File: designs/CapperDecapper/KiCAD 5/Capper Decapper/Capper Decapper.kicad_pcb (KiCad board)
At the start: 4 copper layers, 77.5 x 42.5 mm, 86 parts, among them J1 Pi Control Signals, J2 Motor_Power, J3 Screw_Term, Q1 Q_NMOS_GSD, U1 INA214, U10 74AHC08, U11 DRV8833RTY, U12 INA214, U13 INA214, U14 V7805-1500R, U15 74AHC08, U16 DRV8833RTY, U17 MAX6018BEUR16, U18 INA214, U19 AP1501A, U2 74AHC08, U3 DRV8833RTY, U4 INA214, U5 INA214, U6 74AHC08, U7 DRV8833RTY, U8 INA214, U9 INA214

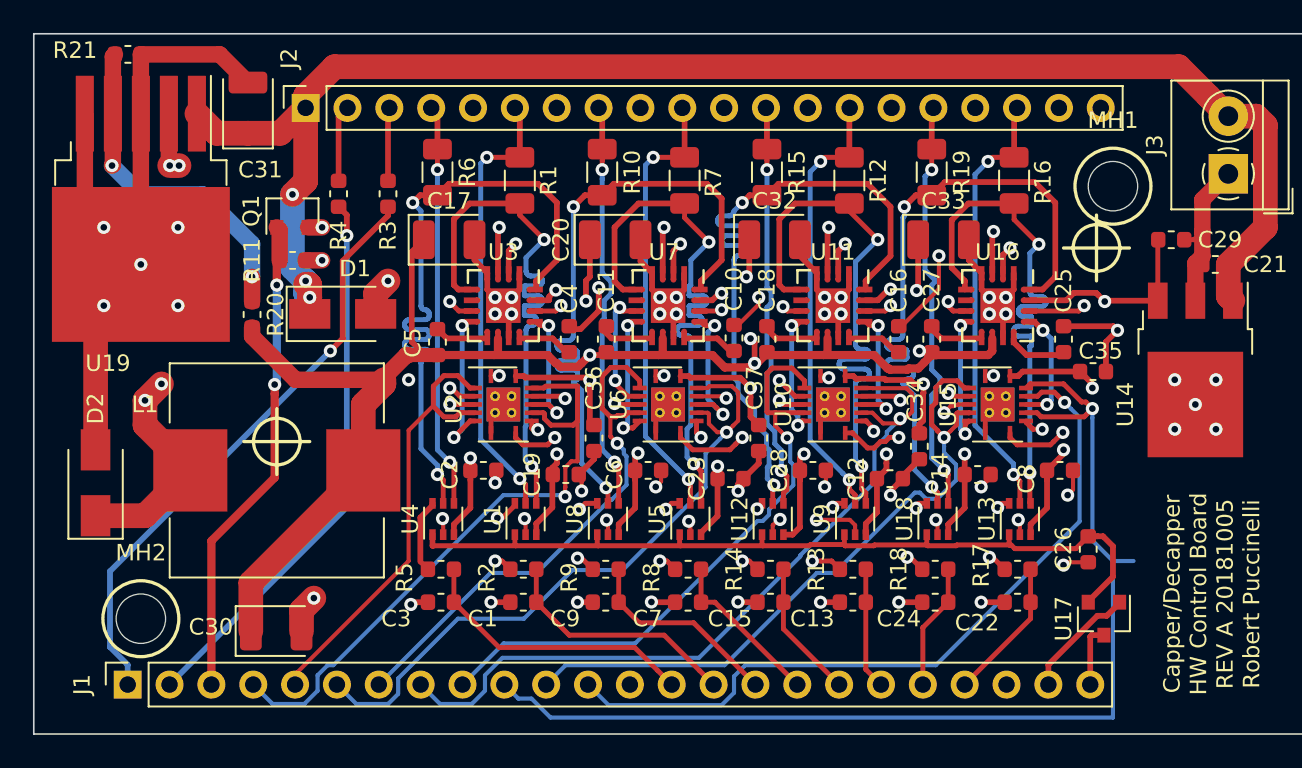
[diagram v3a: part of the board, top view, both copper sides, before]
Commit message: AND gate updated, ordered
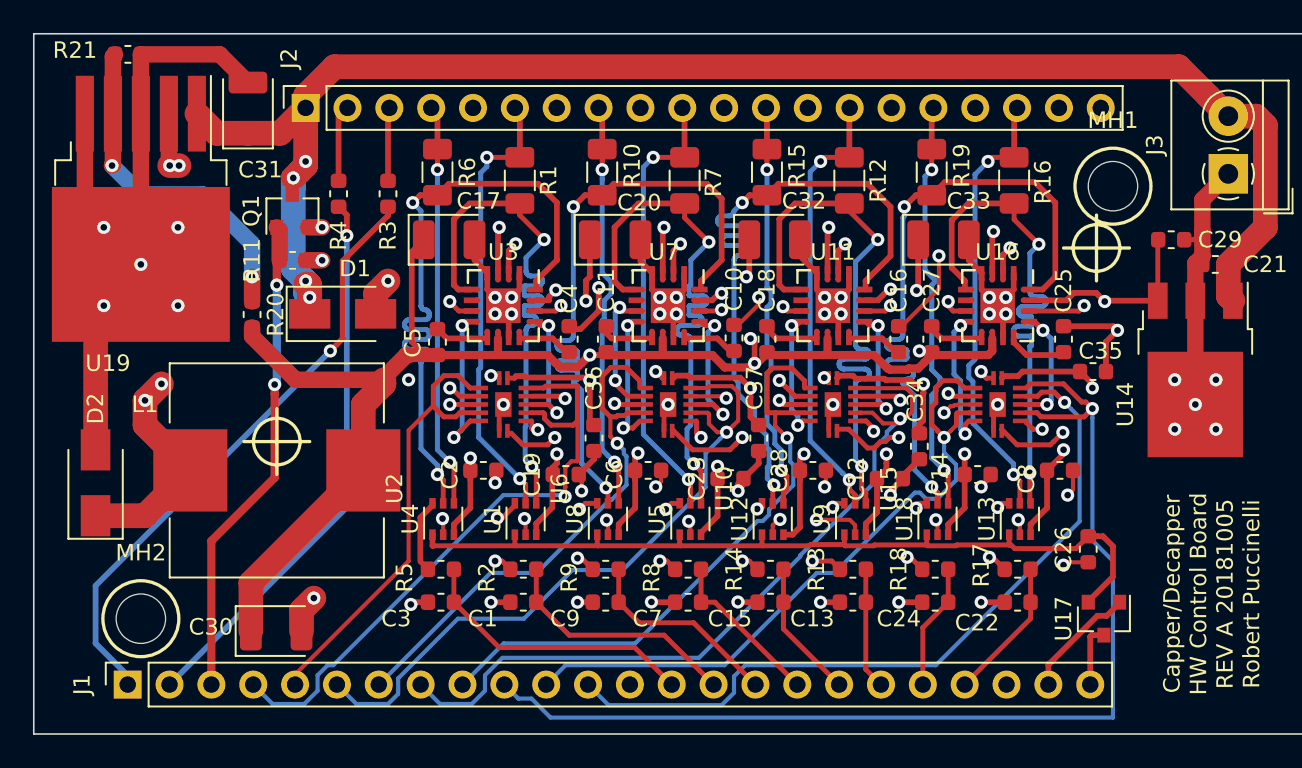
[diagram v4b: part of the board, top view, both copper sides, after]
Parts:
- U10, U15, U2, U6: footprint Package_DFN_QFN:Texas_S-PVQFN-N14_ThermalVias -> CustomFootprints:PVQFN-14
- turned U10 to 270 degrees
- turned U15 to 270 degrees
- turned U2 to 270 degrees
- turned U6 to 270 degrees
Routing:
- net GND: track 160.7 -> 166.3 mm, vias 59 -> 63
- net /5V: track 210.1 -> 212.3 mm
- net /FWD: track 89.3 -> 90.9 mm
- net /REV: track 105.4 -> 106.8 mm
- net /EN7: track 67.4 -> 66.1 mm
- net VBUS: track 94.9 -> 95.9 mm, vias 3 -> 4
- net Net-(J1-Pad1): track 36.4 -> 37.2 mm
- net Net-(U10-Pad8): track 14.5 -> 15.1 mm
